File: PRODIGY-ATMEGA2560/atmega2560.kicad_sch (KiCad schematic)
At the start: 11 parts, among them U1 ATmega2560-16A, U2 TXS0108EPW, Y1 16MHz

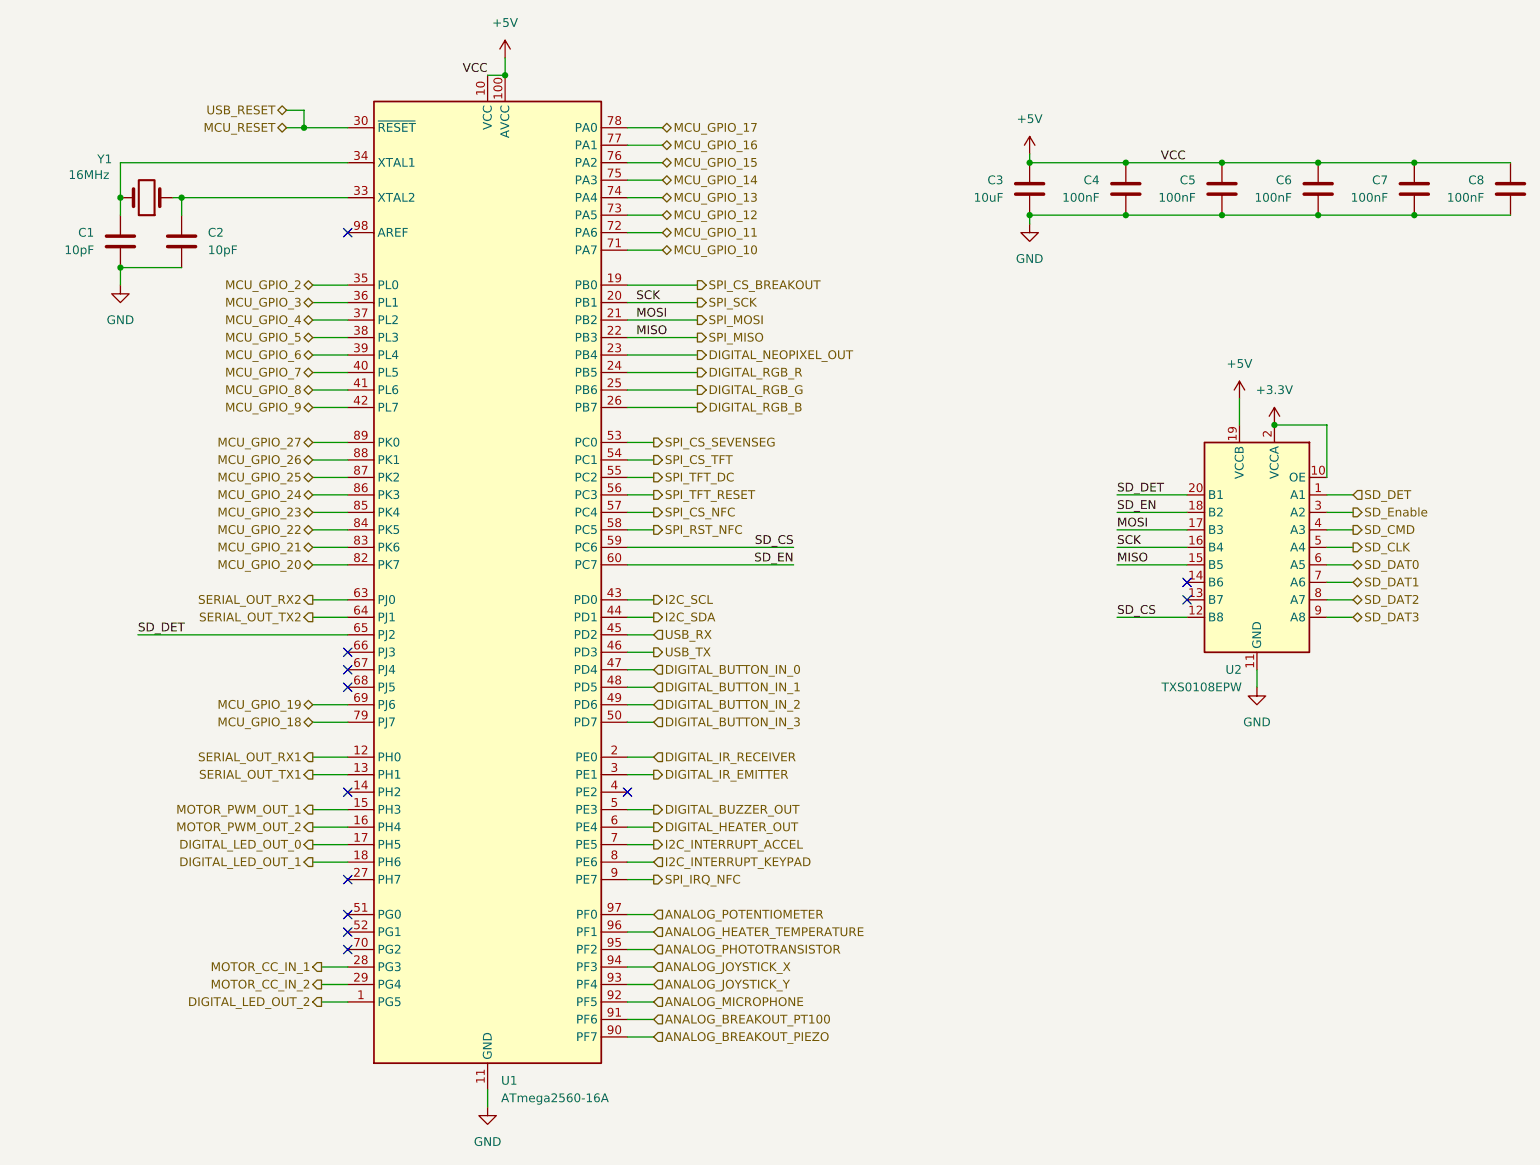
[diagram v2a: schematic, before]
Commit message: ESP32 and ATMEGA bom done.
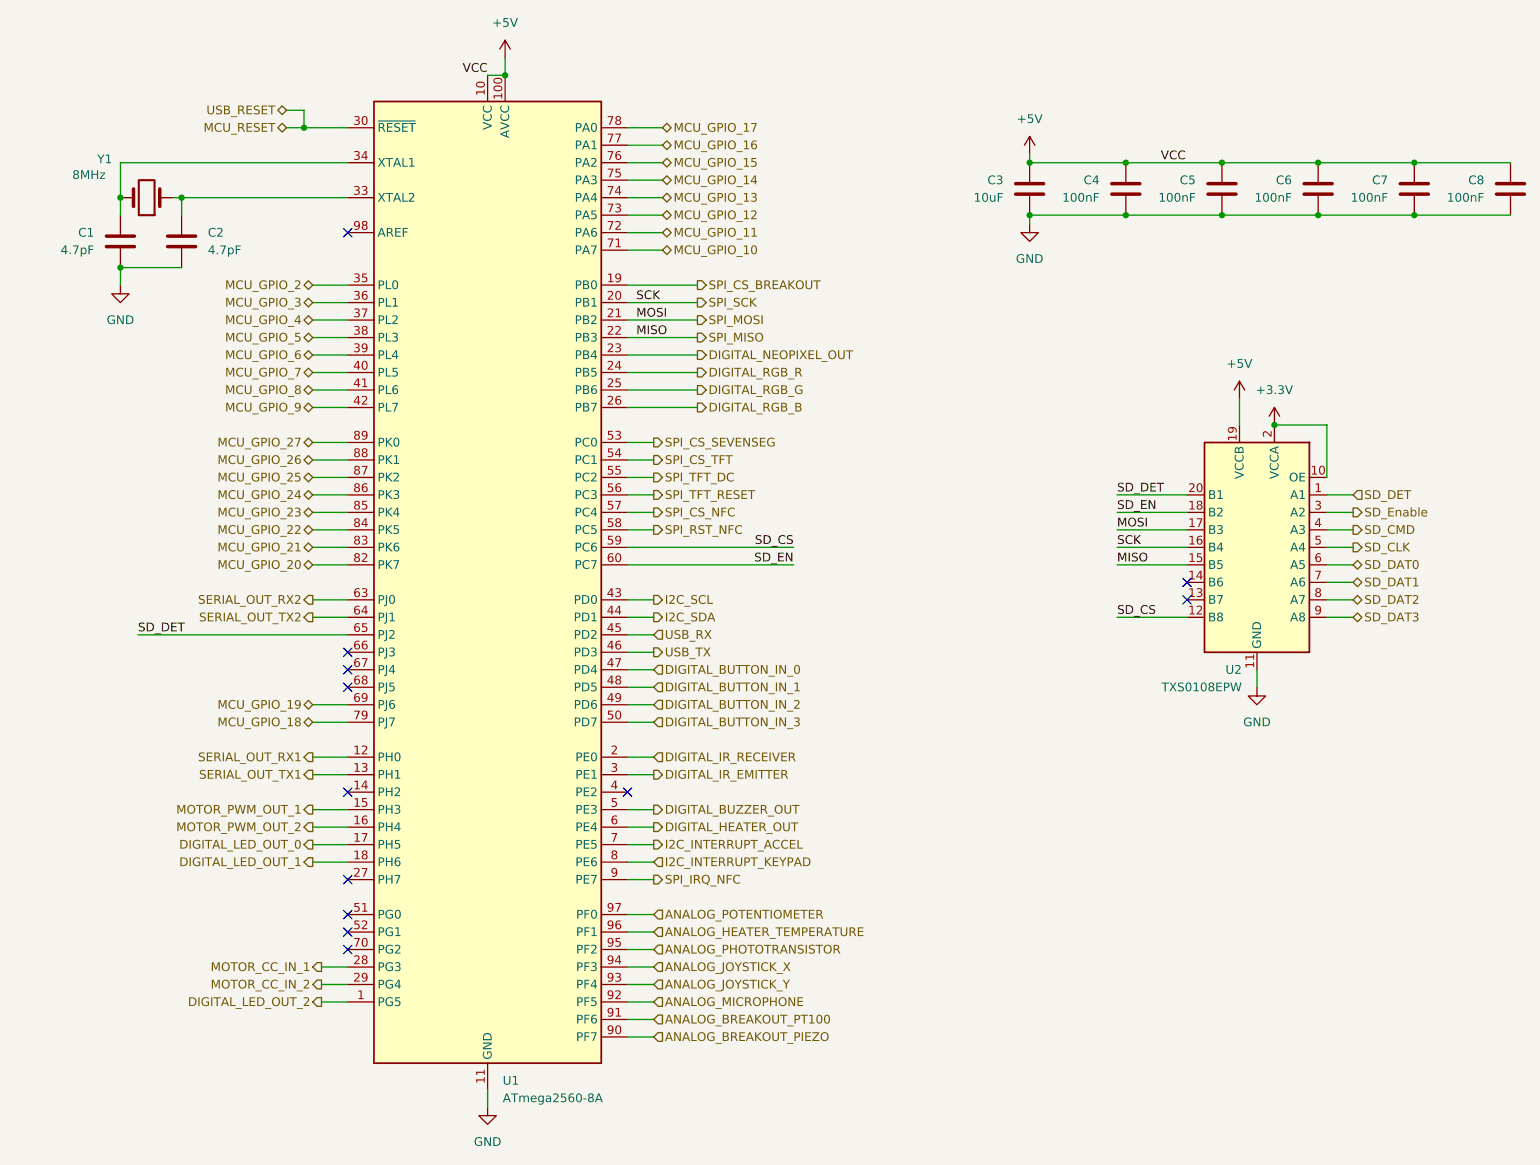
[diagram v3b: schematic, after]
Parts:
- C1, C2: value 10pF -> 4.7pF; TME (none) -> CC0603BRNPO9BN4R7
- C3: TME (none) -> 0603N100J500CT
- C4, C5, C6, C7, C8: TME (none) -> CL10B104KB8NNNC
- U1: value ATmega2560-16A -> ATmega2560-8A; TME (none) -> ATMEGA2560V-8AU
- U2: TME (none) -> TXS0108EPWR
- Y1: value 16MHz -> 8MHz; footprint Crystal:Crystal_SMD_3225-4Pin_3.2x2.5mm -> Crystal:Crystal_SMD_5032-4Pin_5.0x3.2mm; TME (none) -> 8.00M-CFPX104
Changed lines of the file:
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@@
 	(wire
 		(pts
+			(xy 68.58 48.26) (xy 69.85 48.26)
+		)
+		(stroke
+			(width 0)
+			(type default)
+		)
+	)
+	(wire
+		(pts
 			(xy 60.96 58.42) (xy 60.96 60.96)
 		)
@@
 	(wire
 		(pts
-			(xy 68.58 48.26) (xy 69.85 48.26)
-		)
-		(stroke
-			(width 0)
-			(type default)
-		)
-	)
-	(wire
-		(pts
 			(xy 138.43 116.84) (xy 134.62 116.84)
 		)
@@
 			)
 		)
-		(property "Value" "10pF"
+		(property "Value" "4.7pF"
 			(at 73.66 55.8799 0)
 			(effects
@@
 			)
 		)
+		(property "TME" "CC0603BRNPO9BN4R7 "
+			(at 69.85 54.61 0)
+			(effects
+				(font
+					(size 1.27 1.27)
+				)
+				(hide yes)
+			)
+		)
 		(pin "2"
 		)
@@
 			)
 		)
+		(property "TME" "0603N100J500CT "
+			(at 193.04 46.99 0)
+			(effects
+				(font
+					(size 1.27 1.27)
+				)
+				(hide yes)
+			)
+		)
 		(pin "2"
 		)
@@
 			)
 		)
+		(property "TME" "TXS0108EPWR"
+			(at 226.06 99.06 0)
+			(effects
+				(font
+					(size 1.27 1.27)
+				)
+				(hide yes)
+			)
+		)
 		(pin "1"
 		)
@@
 			)
 		)
-		(property "Value" "16MHz"
+		(property "Value" "8MHz"
 			(at 56.388 44.958 0)
 			(effects
@@
 			)
 		)
-		(property "Footprint" "Crystal:Crystal_SMD_3225-4Pin_3.2x2.5mm"
+		(property "Footprint" "Crystal:Crystal_SMD_5032-4Pin_5.0x3.2mm"
 			(at 64.77 48.26 0)
 			(effects
@@
 			)
 		)
+		(property "TME" "8.00M-CFPX104"
+			(at 64.77 48.26 0)
+			(effects
+				(font
+					(size 1.27 1.27)
+				)
+				(hide yes)
+			)
+		)
 		(pin "1"
 		)
@@
 			)
 		)
+		(property "TME" "CL10B104KB8NNNC "
+			(at 262.89 46.99 0)
+			(effects
+				(font
+					(size 1.27 1.27)
+				)
+				(hide yes)
+			)
+		)
 		(pin "2"
 		)
@@
 			)
 		)
+		(property "TME" "CL10B104KB8NNNC "
+			(at 220.98 46.99 0)
+			(effects
+				(font
+					(size 1.27 1.27)
+				)
+				(hide yes)
+			)
+		)
 		(pin "2"
 		)
@@
 			)
 		)
-		(property "Value" "10pF"
+		(property "Value" "4.7pF"
 			(at 57.15 55.8799 0)
 			(effects
@@
 			)
 		)
+		(property "TME" "CC0603BRNPO9BN4R7 "
+			(at 60.96 54.61 0)
+			(effects
+				(font
+					(size 1.27 1.27)
+				)
+				(hide yes)
+			)
+		)
 		(pin "2"
 		)
@@
 			)
 		)
+		(property "TME" "CL10B104KB8NNNC "
+			(at 234.95 46.99 0)
+			(effects
+				(font
+					(size 1.27 1.27)
+				)
+				(hide yes)
+			)
+		)
 		(pin "2"
 		)
@@
 		(fields_autoplaced yes)
 		(property "Reference" "U1"
-			(at 116.2559 176.53 0)
+			(at 116.4941 176.53 0)
 			(effects
 				(font
@@
 			)
 		)
-		(property "Value" "ATmega2560-16A"
-			(at 116.2559 179.07 0)
+		(property "Value" "ATmega2560-8A"
+			(at 116.4941 179.07 0)
 			(effects
 				(font
@@
 			)
 		)
+		(property "TME" "ATMEGA2560V-8AU"
+			(at 114.3 104.14 0)
+			(effects
+				(font
+					(size 1.27 1.27)
+				)
+				(hide yes)
+			)
+		)
 		(pin "1"
 		)
@@
 			)
 		)
+		(property "TME" "CL10B104KB8NNNC "
+			(at 248.92 46.99 0)
+			(effects
+				(font
+					(size 1.27 1.27)
+				)
+				(hide yes)
+			)
+		)
 		(pin "2"
 		)
@@
 			(at 207.01 46.99 0)
 			(effects
+				(font
+					(size 1.27 1.27)
+				)
+				(hide yes)
+			)
+		)
+		(property "TME" "CL10B104KB8NNNC "
+			(at 207.01 46.99 0)
+			(effects

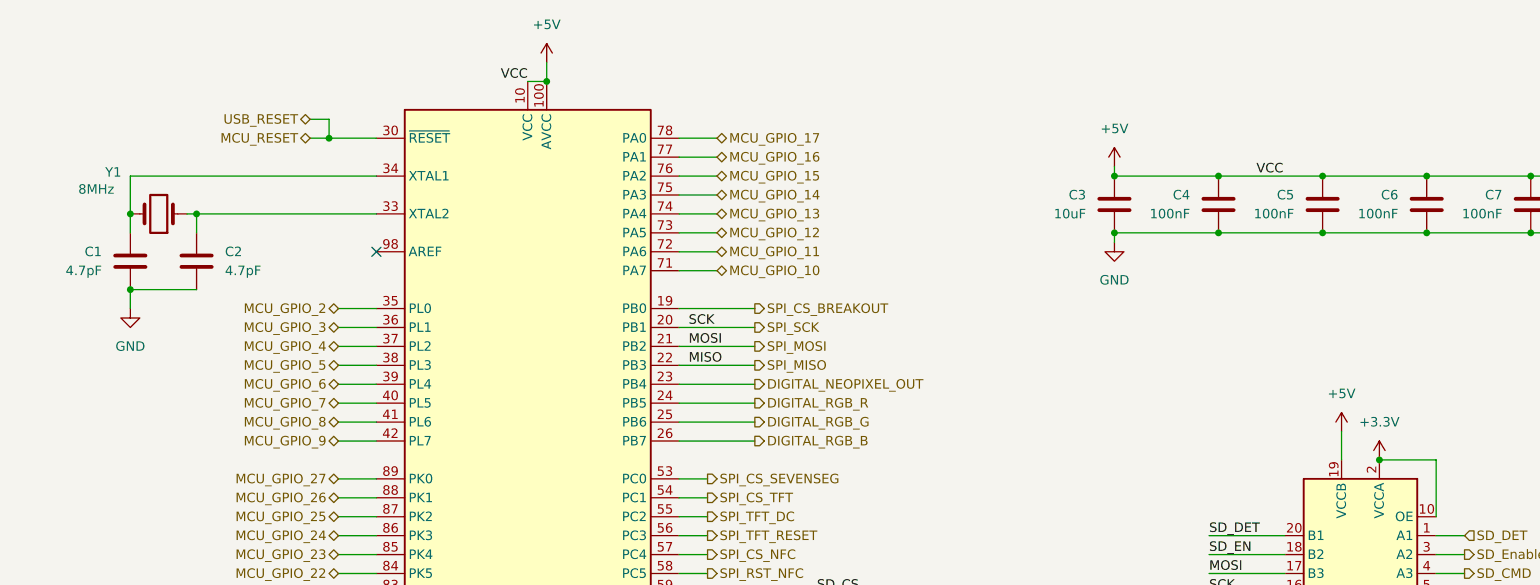
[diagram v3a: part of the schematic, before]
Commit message: Atmega layout done. orientation and alignment testing done. routing started.
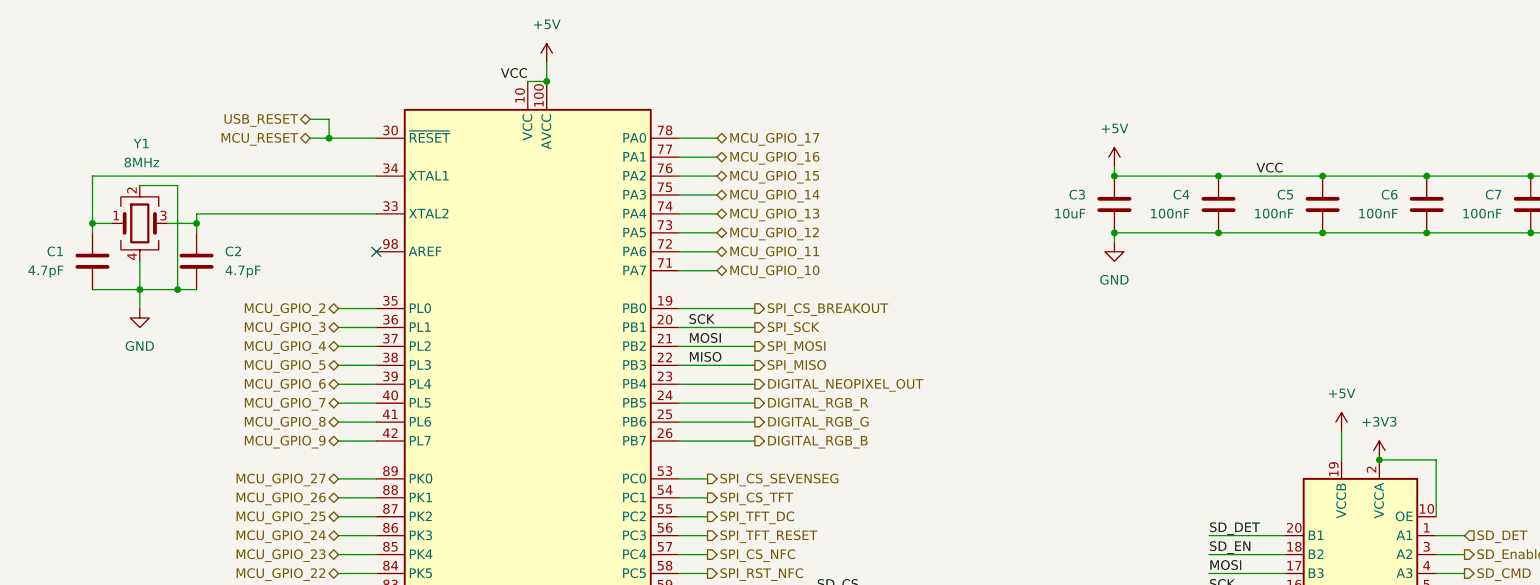
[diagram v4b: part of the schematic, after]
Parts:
- removed Y1: 8MHz, Crystal:Crystal_SMD_5032-4Pin_5.0x3.2mm, symbol Device:Crystal
- added Y1: 8MHz, Crystal:Crystal_SMD_5032-4Pin_5.0x3.2mm, symbol Device:Crystal_GND24
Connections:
- net GND: now also Y1.2, Y1.4
- net at C2.1, U1.33 (XTAL2): now also Y1.3
- net at C1.1, U1.34 (XTAL1): now also Y1.1
- net +3.3V renamed +3V3
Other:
- moved on the sheet: C1

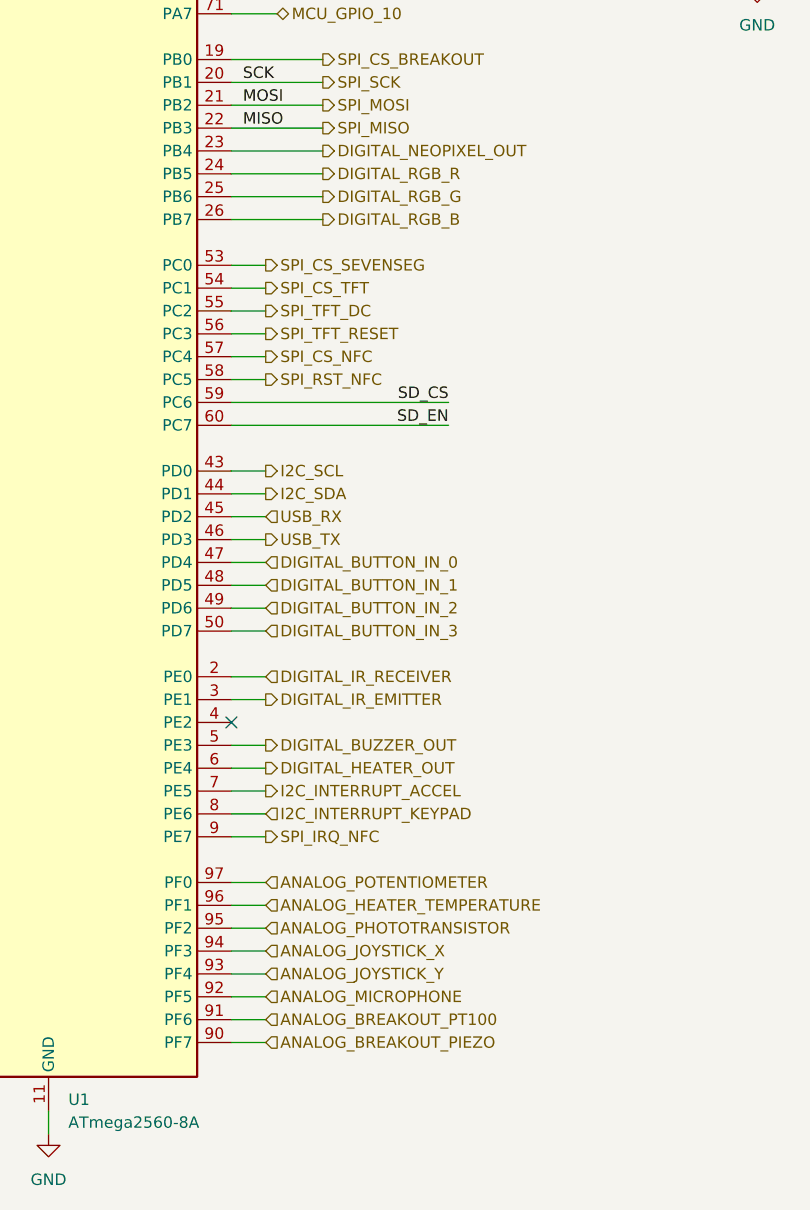
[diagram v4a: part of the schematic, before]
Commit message: vias done, some routing done. analog routing done
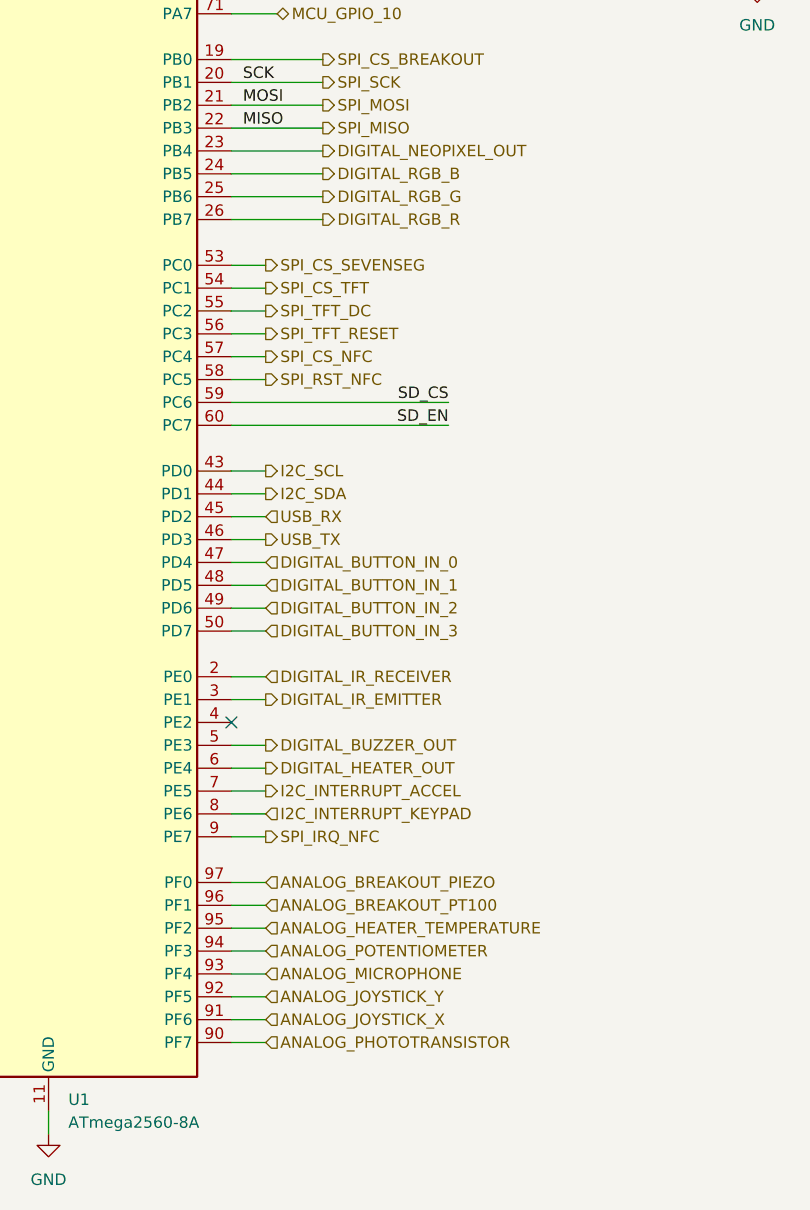
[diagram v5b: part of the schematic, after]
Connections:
- net ANALOG_BREAKOUT_PIEZO: now also U1.97 (PF0); no longer U1.90 (PF7)
- net ANALOG_BREAKOUT_PT100: now also U1.96 (PF1); no longer U1.91 (PF6)
- net ANALOG_HEATER_TEMPERATURE: now also U1.95 (PF2); no longer U1.96 (PF1)
- net ANALOG_JOYSTICK_X: now also U1.91 (PF6); no longer U1.94 (PF3)
- net ANALOG_JOYSTICK_Y: now also U1.92 (PF5); no longer U1.93 (PF4)
- net ANALOG_MICROPHONE: now also U1.93 (PF4); no longer U1.92 (PF5)
- net ANALOG_PHOTOTRANSISTOR: now also U1.90 (PF7); no longer U1.95 (PF2)
- net ANALOG_POTENTIOMETER: now also U1.94 (PF3); no longer U1.97 (PF0)
- net DIGITAL_RGB_B: now also U1.24 (PB5); no longer U1.26 (PB7)
- net DIGITAL_RGB_R: now also U1.26 (PB7); no longer U1.24 (PB5)

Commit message: major routing done on atmega board.
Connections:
- net ANALOG_BREAKOUT_PIEZO: now also U1.90 (PF7); no longer U1.97 (PF0)
- net ANALOG_BREAKOUT_PT100: now also U1.91 (PF6); no longer U1.96 (PF1)
- net ANALOG_HEATER_TEMPERATURE: now also U1.92 (PF5); no longer U1.95 (PF2)
- net ANALOG_JOYSTICK_X: now also U1.96 (PF1); no longer U1.91 (PF6)
- net ANALOG_JOYSTICK_Y: now also U1.95 (PF2); no longer U1.92 (PF5)
- net ANALOG_MICROPHONE: now also U1.94 (PF3); no longer U1.93 (PF4)
- net ANALOG_PHOTOTRANSISTOR: now also U1.97 (PF0); no longer U1.90 (PF7)
- net ANALOG_POTENTIOMETER: now also U1.93 (PF4); no longer U1.94 (PF3)
- net DIGITAL_RGB_B: now also U1.15 (PH3); no longer U1.24 (PB5)
- net DIGITAL_RGB_G: now also U1.16 (PH4); no longer U1.25 (PB6)
- net DIGITAL_RGB_R: now also U1.24 (PB5); no longer U1.26 (PB7)
- net MCU_GPIO_10: now also U1.83 (PK6); no longer U1.71 (PA7)
- net MCU_GPIO_11: now also U1.36 (PL1); no longer U1.72 (PA6)
- net MCU_GPIO_12: now also U1.74 (PA4); no longer U1.73 (PA5)
- net MCU_GPIO_13: now also U1.39 (PL4); no longer U1.74 (PA4)
- net MCU_GPIO_14: now also U1.77 (PA1); no longer U1.75 (PA3)
- net MCU_GPIO_16: now also U1.72 (PA6); no longer U1.77 (PA1)
- net MCU_GPIO_17: now also U1.86 (PK3); no longer U1.78 (PA0)
- net MCU_GPIO_2: now also U1.89 (PK0); no longer U1.35 (PL0)
- net MCU_GPIO_20: now also U1.73 (PA5); no longer U1.82 (PK7)
- net MCU_GPIO_21: now also U1.71 (PA7); no longer U1.83 (PK6)
- net MCU_GPIO_23: now also U1.78 (PA0); no longer U1.85 (PK4)
- net MCU_GPIO_24: now also U1.41 (PL6); no longer U1.86 (PK3)
- net MCU_GPIO_25: now also U1.82 (PK7); no longer U1.87 (PK2)
- net MCU_GPIO_26: now also U1.40 (PL5); no longer U1.88 (PK1)
- net MCU_GPIO_27: now also U1.85 (PK4); no longer U1.89 (PK0)
- net MCU_GPIO_3: now also U1.88 (PK1); no longer U1.36 (PL1)
- net MCU_GPIO_4: now also U1.87 (PK2); no longer U1.37 (PL2)
- net MCU_GPIO_5: now also U1.37 (PL2); no longer U1.38 (PL3)
- net MCU_GPIO_6: now also U1.38 (PL3); no longer U1.39 (PL4)
- net MCU_GPIO_7: now also U1.75 (PA3); no longer U1.40 (PL5)
- net MCU_GPIO_8: now also U1.42 (PL7); no longer U1.41 (PL6)
- net MCU_GPIO_9: now also U1.35 (PL0); no longer U1.42 (PL7)
- net MOTOR_PWM_OUT_1: now also U1.26 (PB7); no longer U1.15 (PH3)
- net MOTOR_PWM_OUT_2: now also U1.25 (PB6); no longer U1.16 (PH4)
- net SD_CLK: now also U2.1 (A1); no longer U2.5 (A4)
- net SD_CS: now also U1.19 (PB0), U2.18 (B2); no longer U1.59 (PC6), U2.12 (B8)
- net SD_DAT1: now also U2.5 (A4); no longer U2.7 (A6)
- net SD_DAT2: now also U2.7 (A6); no longer U2.8 (A7)
- net SD_DAT3: now also U2.3 (A2); no longer U2.9 (A8)
- net SD_DET: now also U2.8 (A7); no longer U1.65 (PJ2), U2.1 (A1), U2.20 (B1)
- net SD_EN: now also U1.65 (PJ2), U2.12 (B8); no longer U1.60 (PC7), U2.18 (B2)
- net SD_Enable: now also U2.9 (A8); no longer U2.3 (A2)
- net SPI_CS_BREAKOUT: now also U1.59 (PC6); no longer U1.19 (PB0)
- net SPI_SCK: now also U2.20 (B1); no longer U2.16 (B4)
- net SD_DET_5V: now reaches U2.13 (B7)
- net SD_DET_5V: now also U1.60 (PC7)
